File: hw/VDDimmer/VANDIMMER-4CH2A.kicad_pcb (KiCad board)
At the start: 2 copper layers, 100 x 80 mm, 100 parts, among them J1 USB-C 16P, J10 A2 V+SEL VIN/5V, J11 BTN1, J12 BTN2, J13 EXP 3V3/GND/SDA/SCL/EN/IO0, J14 UART1 3V3/GND/TX/RX, J2 VIN 9-24V, J3 CH1 V+/LED-, J4 CH2 V+/LED-, J5 CH3 V+/LED-, J6 CH4 V+/LED-, J7 ADDR1 V+/D/CLK/GND, J8 ADDR2 V+/D/CLK/GND, J9 A1 V+SEL VIN/5V, Q1 20N06, Q2 20N06, Q3 20N06, Q4 20N06, Q5 SUD50P06-15, U1 ESP32-S3-WROOM-1U-N16, U2 AP64350SP-13, U3 AMS1117-3.3, U4 74HCT125, U5 74HCT125

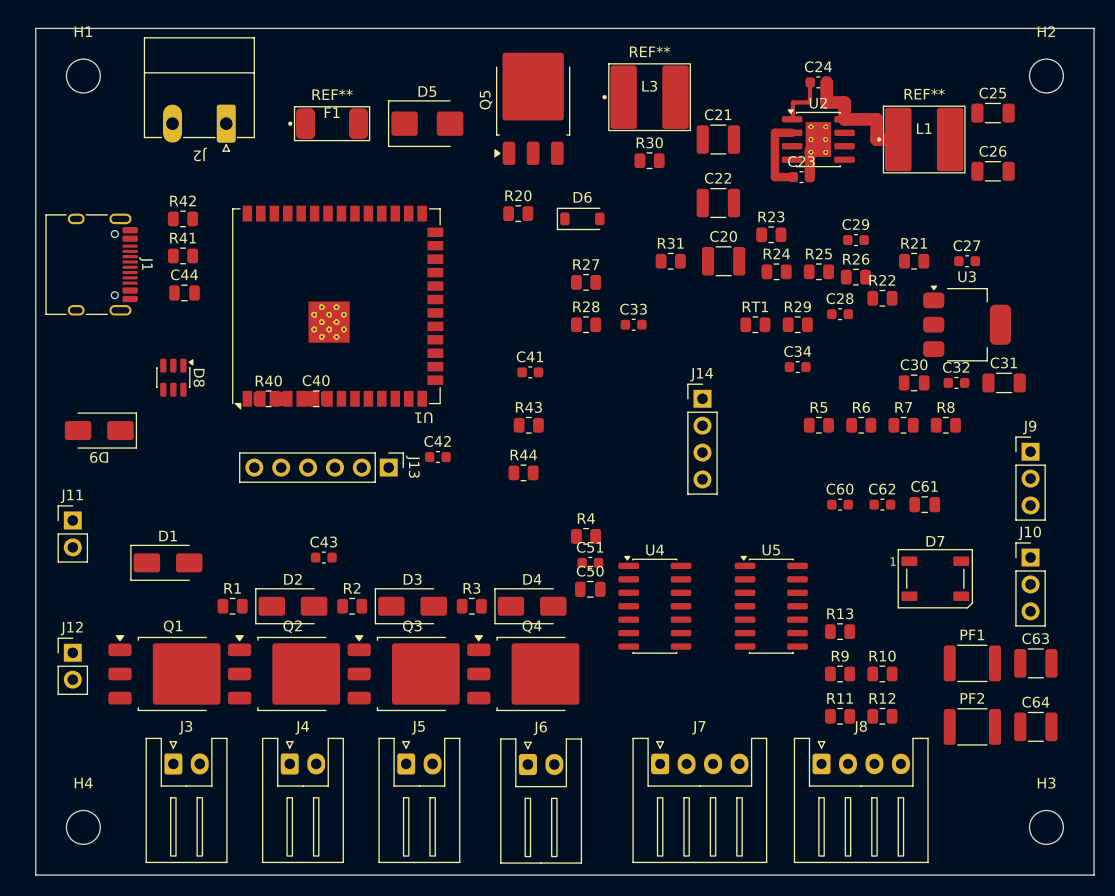
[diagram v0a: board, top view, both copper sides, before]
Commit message: Fix placement/trace coordinate desync, re-verify buck routing
The Update Footprints from Library pass re-anchored 30 footprints by
footprint-type-specific offsets (0 for symmetric mounting holes,
-2.05/-3.5 for SOIC-8 and 0603, +2.0 for the XH connectors), and also
changed rotations on Q5, D8, D9 and J13.

Traces routed during that window were placed in the shifted frame, so
they were correctly connected to the pads but at coordinates 2.05/3.5
away from the design intent. Restoring the parts desynchronised them.

All 100 footprints now verified against the intended placement table
(0 mismatches) and all 13 buck traces rebuilt against pad coordinates
read back from the board rather than assumed.

Hot loop re-measured from real pads and real copper: 14.31 mm2
(was reported 13.93 using the exposed-pad centre; this uses the
nearest exposed-pad contact, which is the honest junction point).
DRC 0 errors.

Co-Authored-By: Claude Opus 5 (1M context) <noreply@anthropic.com>
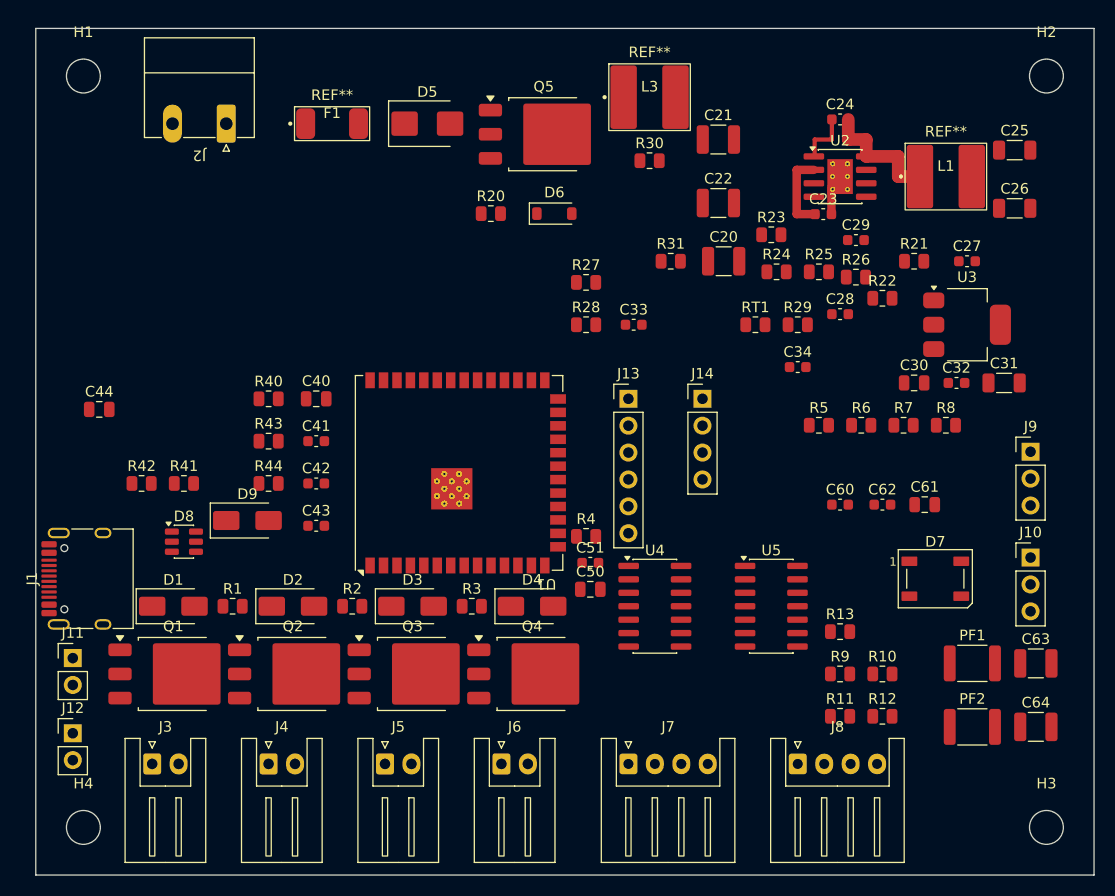
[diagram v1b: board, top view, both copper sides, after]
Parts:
- moved J1 29.7 mm to (105.3, 112.0), turned to 90 degrees
- moved R42 25.3 mm to (110.0, 103.0)
- moved R43 24.6 mm to (122.0, 99.0)
- moved R44 24.1 mm to (122.0, 103.0)
- moved J13 23.6 mm to (156.0, 95.0), turned to 0 degrees
- moved R41 21.5 mm to (114.0, 103.0)
- moved C41 21.2 mm to (126.5, 99.0)
- moved U1 19.6 mm to (140.0, 102.0)
- moved D9 16.4 mm to (120.0, 106.5), turned to 0 degrees
- moved D8 15.5 mm to (114.0, 108.5), turned to 0 degrees
- moved C44 13.6 mm to (106.0, 96.0)
- moved J11 13.0 mm to (103.5, 119.5)
- moved C42 11.8 mm to (126.5, 103.0)
- moved J12 7.60 mm to (103.5, 126.6)
- moved D1 4.13 mm to (113.0, 114.6)
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
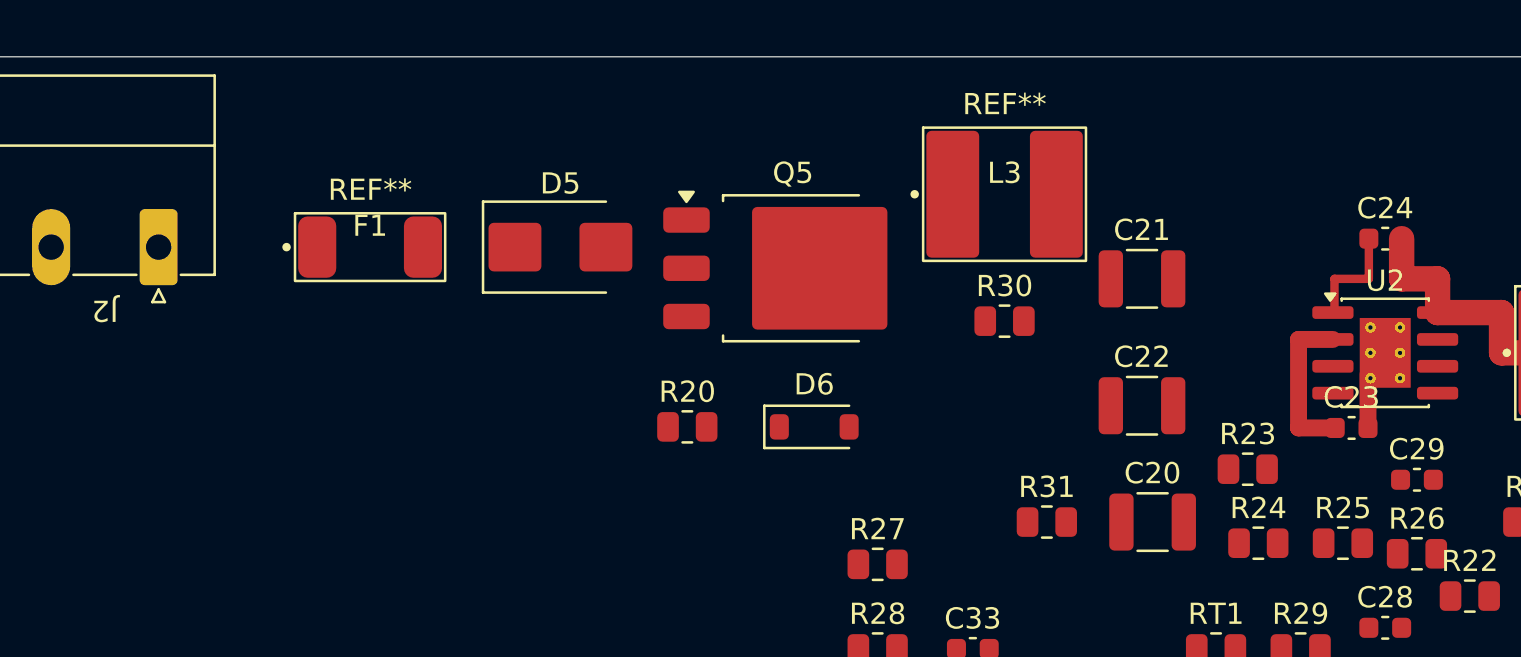
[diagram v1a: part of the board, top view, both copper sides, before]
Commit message: Route input protection chain and VIN_BUCK distribution
C23 -> 0402 (100nF/25V): hot loop 14.31 -> 13.31 mm2, 11% margin.
VIN corridor necked to 0.6mm to hold clearance to the GND return.

Routed: VIN_RAW (J2->F1), VIN_FUSED (F1->D5->Q5 tab, routed above D5
to clear its GND pad), QREV_G (Q5 gate -> R20 -> D6), VIN_BUCK
distribution (R30/L3 -> C21/C22 -> R31 -> R23 -> buck), VIN_DAMP.

0 real DRC errors. 24-28 reported errors are C23's 4 phantom pads,
re-injected by update_pcb_from_schematic; place_component does not
have this bug but produces footprints with no schematic identity,
so it cannot carry nets.

Co-Authored-By: Claude Opus 5 (1M context) <noreply@anthropic.com>
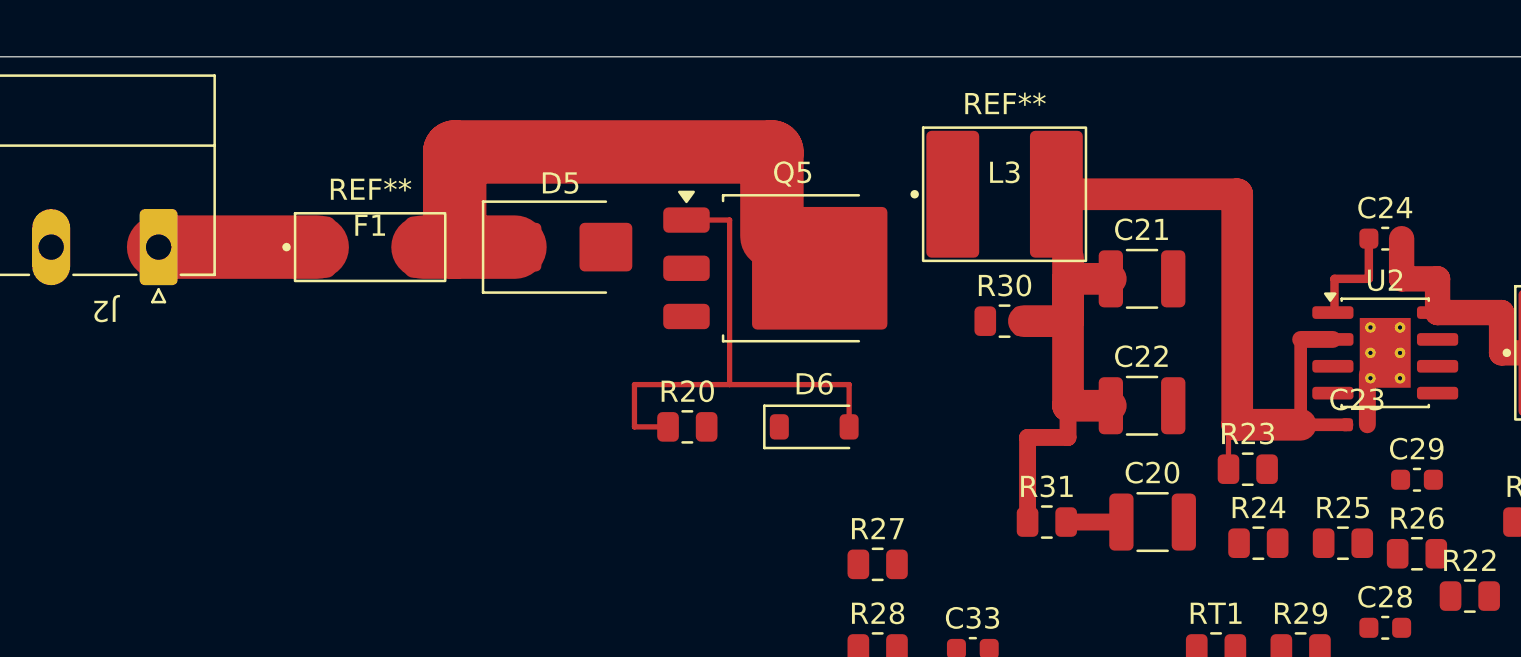
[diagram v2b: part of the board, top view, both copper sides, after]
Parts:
- C23: value 100nF/50V -> 100nF/25V; footprint Capacitor_SMD:C_0603_1608Metric -> Capacitor_SMD:C_0402_1005Metric
- moved C23 0.30 mm to (174.7, 77.4)
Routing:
- net /Power/VIN_BUCK: track 7.54 -> 55.3 mm
- net /Power/VIN_FUSED: track 0.00 -> 27.8 mm
- net /Power/QREV_G: track 0.00 -> 25.6 mm
- net /Power/VIN_RAW: track 0.00 -> 7.50 mm
- net /Power/VIN_DAMP: track 0.00 -> 2.61 mm

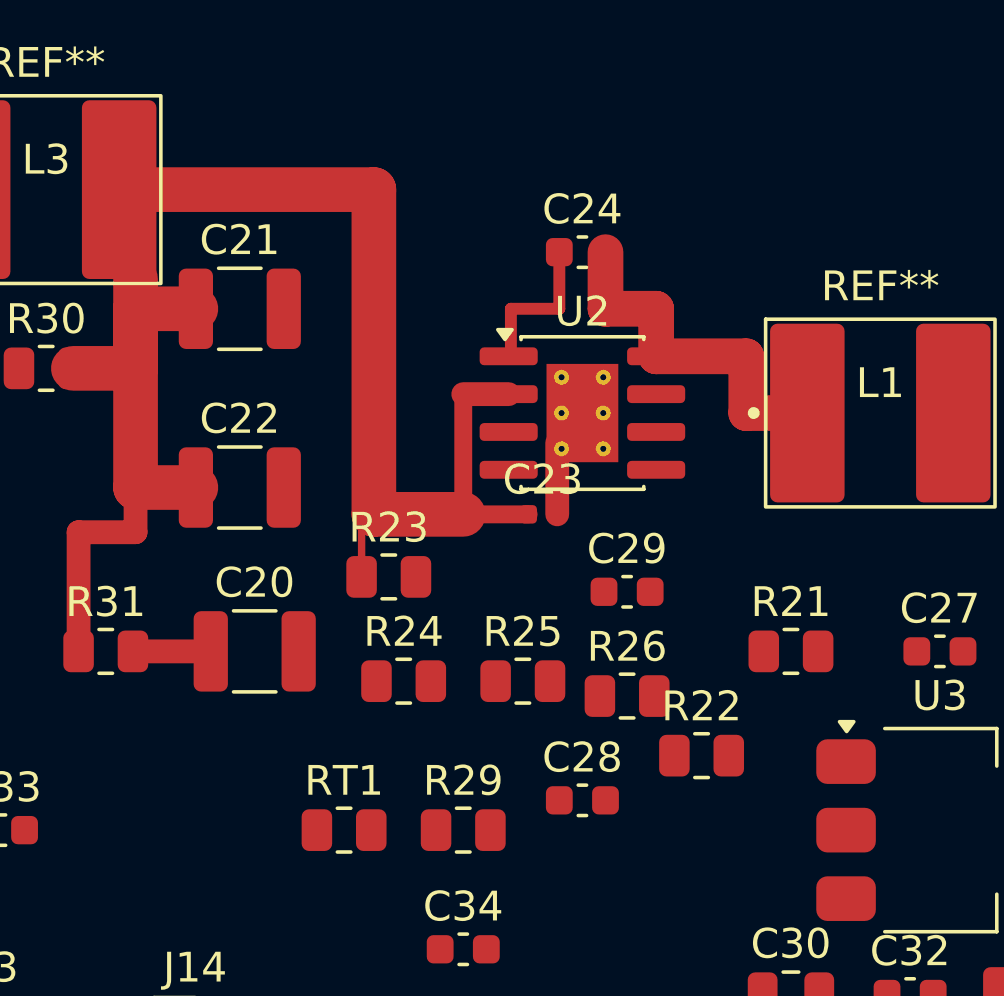
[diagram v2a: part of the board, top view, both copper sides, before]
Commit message: Swap buck to AP63301WU-7: hot loop 13.31 -> 4.60 mm2
The AP64350's SO-8EP pinout (VIN pin2 / GND pin7 diagonal, BST and SW
between them) has no valid 2-layer routing: Cin above the IC forces a
VIN/BST crossing, Cin below encloses EN and RT with no escape that
doesn't either break the 8.5.3 keepout or push the hot loop to
16.5 mm2. Measured, not estimated.

AP63301WU-7 (C2158003, TSOT-23-6, 3.8-32V, 3A, 500kHz, spread
spectrum) has VIN (pin3) and GND (pin4) adjacent on the bottom edge.
Cin bridges them directly from below:

  hot loop  4.60 mm2  (target <15, 69% margin)
  vias in loop 0
  BST cap bridges pin6/pin5, adjacent on the right edge
  FB and EN on the free left edge, nothing enclosing them

Internally compensated at fixed 500kHz, so R25 (RT_SET), R26/C28
(COMP network) and C29 are deleted - 4 fewer parts and 3 fewer nets.
500kHz unchanged so L1 stays 10uH and C25/C26 unchanged. FB divider
unchanged: 52.3k/10k with 0.8V ref = 4.98V.

D5 SMBJ20A -> SMBJ18A (C19077573, Preferred, 42k stock): 29.2V clamp
sits under the AP63301's 32V abs max; SMBJ20A's 32.4V did not.

New symbol VANDIMMER:AP63301 authored. ERC 0/0, DRC 0 real errors.
Remaining 540 DRC errors are 24 Konnect phantom pads on U2 and C23.

Co-Authored-By: Claude Opus 5 (1M context) <noreply@anthropic.com>
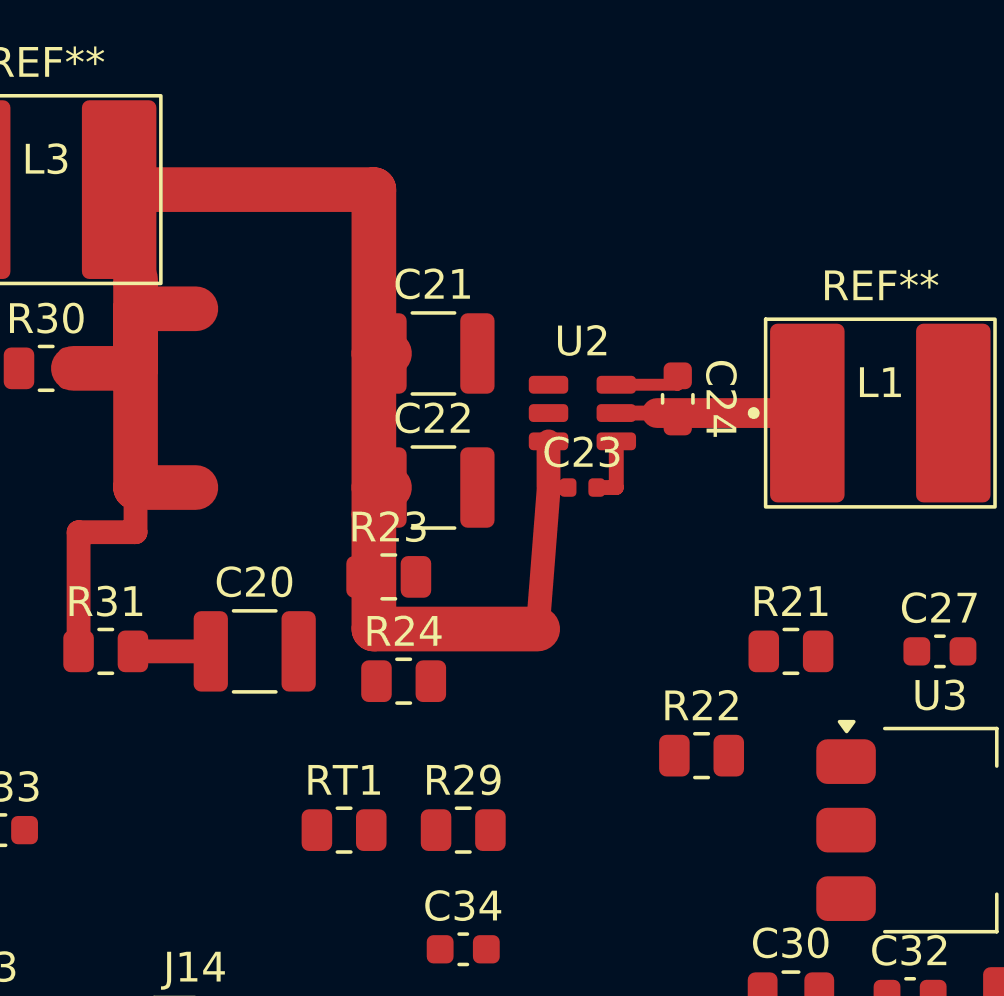
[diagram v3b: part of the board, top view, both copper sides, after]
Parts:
- removed C28: 2.2nF, Capacitor_SMD:C_0603_1608Metric
- removed C29: 100pF, Capacitor_SMD:C_0603_1608Metric
- removed R25: 100k, Resistor_SMD:R_0805_2012Metric
- removed R26: 10k, Resistor_SMD:R_0805_2012Metric
- D5: value SMBJ20A -> SMBJ18A
- U2: value AP64350SP-13 -> AP63301WU-7; footprint Package_SO:SOIC-8-1EP_3.9x4.9mm_P1.27mm_EP2.41x3.3mm_ThermalVias -> Package_TO_SOT_SMD:TSOT-23-6
- moved C21 6.67 mm to (171.0, 72.0)
- moved C22 6.50 mm to (171.0, 76.5)
- moved C24 5.87 mm to (179.2, 73.5), turned to -90 degrees
- moved C23 1.60 mm to (176.0, 76.5)
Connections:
- U2 pad 1: /Power/BST -> /Power/FB
- U2 pad 2: /Power/VIN_BUCK -> /Power/EN_BUCK
- U2 pad 3: /Power/EN_BUCK -> /Power/VIN_BUCK
- U2 pad 4: /Power/RT_SET -> GND
- U2 pad 5: /Power/FB -> /Power/SW
- U2 pad 6: /Power/COMP -> /Power/BST
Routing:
- net /Power/VIN_BUCK: track 55.3 -> 61.8 mm
- net /Power/SW: track 12.2 -> 6.71 mm
- net /Power/BST: track 5.12 -> 2.36 mm

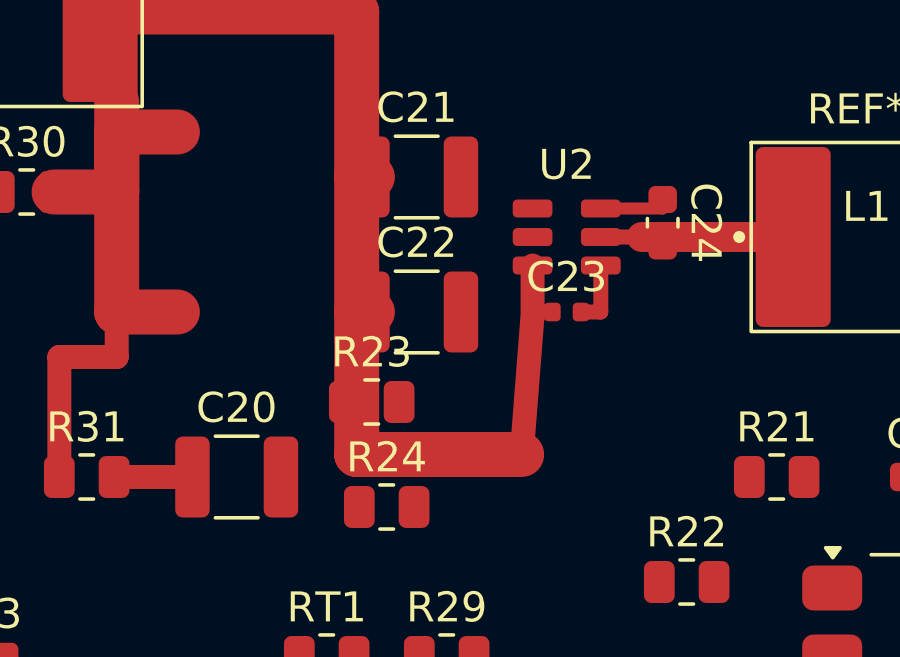
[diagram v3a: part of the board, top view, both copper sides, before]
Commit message: Phantom pads cleared, DRC 0 errors, placement verified
Targeted Update Footprint on U2 and C23 removed all 24 phantom pads
without re-anchoring anything: 96/96 footprints still match the
intended placement table exactly.

Fixed last real DRC error: VIN_BUCK trunk clipped R23's EN pad;
dodged the segment to x=168.

Verified state:
  phantom pads         0
  DRC                  0 errors
  hot loop             4.60 mm2 (69% margin), 0 vias
  unconnected items    197 (routing still to do)

Co-Authored-By: Claude Opus 5 (1M context) <noreply@anthropic.com>
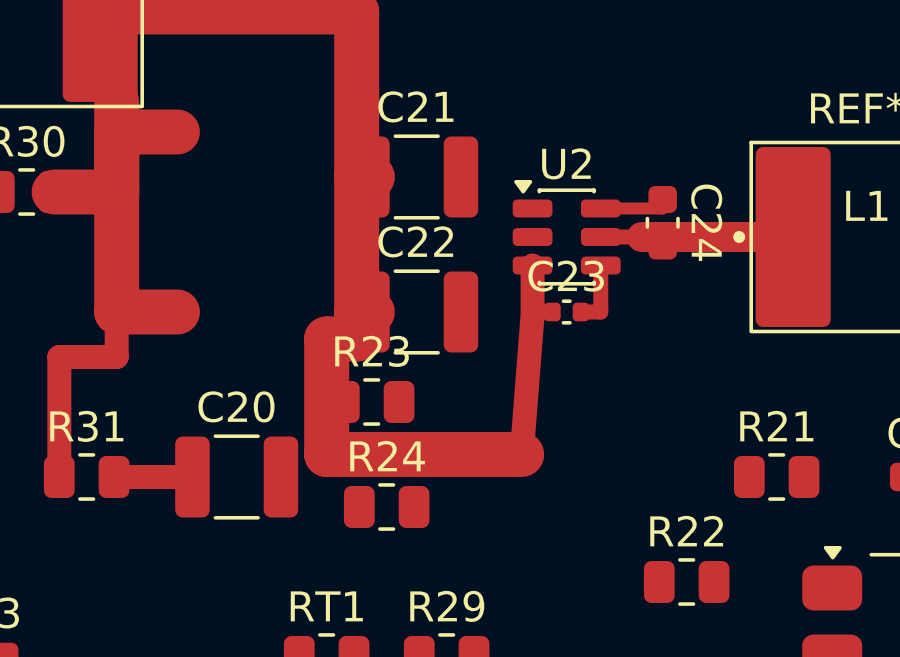
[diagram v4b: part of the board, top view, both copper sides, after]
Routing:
- net /Power/VIN_BUCK: track 61.8 -> 63.8 mm
